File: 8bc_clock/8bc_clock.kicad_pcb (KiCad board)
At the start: 2 copper layers, 61 x 63.5 mm, 27 parts, among them J1 Conn_01x05_Pin, SW1 SW_SPDT, SW2 SW_DIP_x01, U1 ICM7555xP, U2 ICM7555xP, U3 ICM7555xP, U4 74LS04, U5 74LS08, U6 74LS32

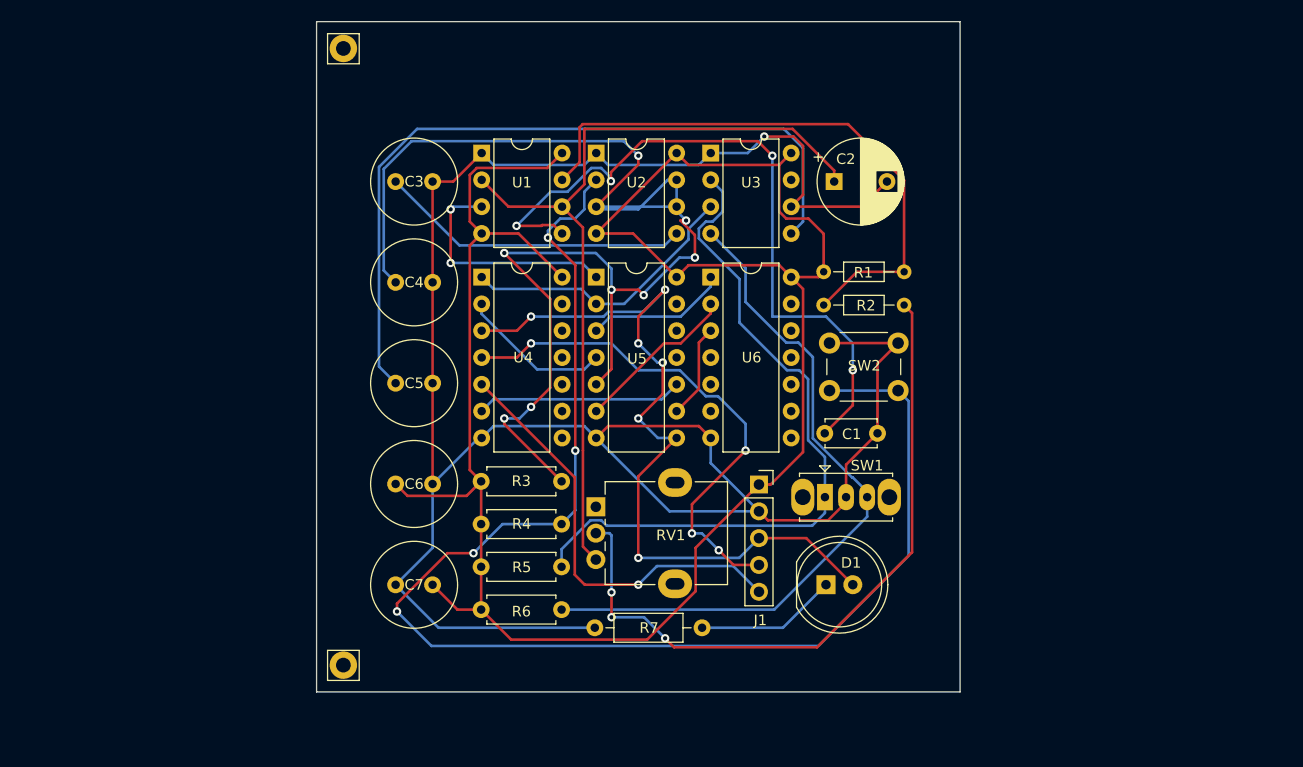
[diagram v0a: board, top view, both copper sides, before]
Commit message: fixed clock circuit error
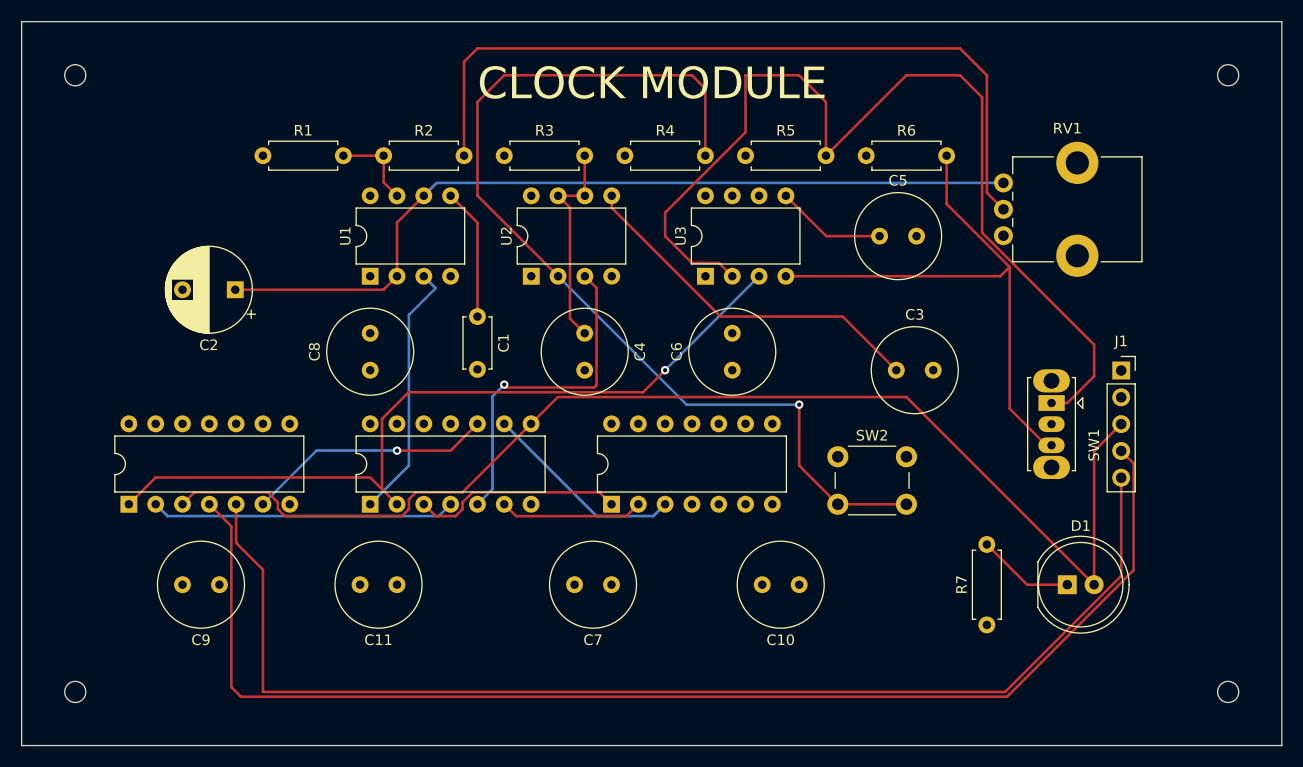
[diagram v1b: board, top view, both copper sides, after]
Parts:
- removed the REF** at (106.7, 53.3)
- removed the REF*** at (106.7, 111.8)
- added C10: 100n, Capacitor_THT:C_Radial_D8.0mm_H7.0mm_P3.50mm, F.Cu at (149.9, 104.1)
- added C11: 100n, Capacitor_THT:C_Radial_D8.0mm_H7.0mm_P3.50mm, F.Cu at (111.8, 104.1)
- added C8: 100n, Capacitor_THT:C_Radial_D8.0mm_H7.0mm_P3.50mm, F.Cu at (109.2, 83.8)
- added C9: 100n, Capacitor_THT:C_Radial_D8.0mm_H7.0mm_P3.50mm, F.Cu at (94.9, 104.1)
- added REF**: MountingHole_2mm, MountingHole:MountingHole_2mm, F.Cu at (81.3, 114.3)
- added REF**: MountingHole_2mm, MountingHole:MountingHole_2mm, F.Cu at (190.5, 55.9)
- added REF**: MountingHole_2mm, MountingHole:MountingHole_2mm, F.Cu at (190.5, 114.3)
- added REF***: MountingHole_2mm, MountingHole:MountingHole_2mm, F.Cu at (81.3, 55.9)
- C1, C3: value 0.01uF -> 10n
- C2: value 1uF -> 1u
- C4, C5, C6, C7: value 0.1uF -> 100n
- R1, R2: footprint Resistor_THT:R_Axial_DIN0204_L3.6mm_D1.6mm_P7.62mm_Horizontal -> Resistor_THT:R_Axial_DIN0207_L6.3mm_D2.5mm_P7.62mm_Horizontal
- R7: value 200 -> 220; footprint Resistor_THT:R_Axial_DIN0207_L6.3mm_D2.5mm_P10.16mm_Horizontal -> Resistor_THT:R_Axial_DIN0207_L6.3mm_D2.5mm_P7.62mm_Horizontal
- RV1: footprint Potentiometer_THT:Potentiometer_Alpha_RD901F-40-00D_Single_Vertical -> Potentiometer_THT:Potentiometer_Bourns_PTV09A-1_Single_Vertical
- moved C2 57.7 mm to (96.4, 76.2), turned to 180 degrees
- moved R6 56.4 mm to (156.2, 63.5)
- moved R1 54.2 mm to (99.1, 63.5)
- moved C3 50.7 mm to (159.1, 83.8)
- moved C5 47.9 mm to (157.5, 71.1)
- moved RV1 46.4 mm to (169.2, 71.1)
- moved R5 46.3 mm to (144.8, 63.5)
- moved R2 44.0 mm to (110.5, 63.5)
- moved U4 39.7 mm to (86.4, 96.5), turned to 90 degrees
- moved R4 37.5 mm to (133.3, 63.5)
- moved R7 37.1 mm to (167.6, 108.0), turned to 90 degrees
- moved J1 36.0 mm to (180.4, 83.8)
- moved C1 34.7 mm to (119.4, 78.7), turned to -90 degrees
- moved C6 33.7 mm to (143.5, 83.8), turned to 90 degrees
- moved R3 30.9 mm to (121.9, 63.5)
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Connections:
- C7 pad 1: GND -> +5V
- C7 pad 2: +5V -> GND
- U2 pad 3: Net-(U2-DIS) -> Net-(U2-Q)
- U5 pad 5: Net-(U2-DIS) -> Net-(U2-Q)
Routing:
- net GND: track 205.7 -> 0.00 mm, vias 1 -> 0
- net +5V: track 194.7 -> 0.00 mm
- net Net-(U2-DIS): track 128.9 -> 20.4 mm, vias 8 -> 0
- net HLT: track 41.3 -> 114.0 mm, vias 1 -> 0
- net !CLK: track 48.8 -> 120.8 mm, vias 4 -> 0
- net Net-(U3-CV): track 72.1 -> 10.5 mm
- net Net-(U1-CV): track 68.1 -> 12.5 mm, vias 4 -> 0
- net Net-(U3-Q): track 27.2 -> 75.5 mm, vias 0 -> 1
- net Net-(U1-DIS): track 56.3 -> 8.14 mm
- net CLK: track 74.6 -> 117.0 mm, vias 6 -> 0
- net Net-(U2-TR): track 132.3 -> 94.5 mm, vias 4 -> 1
- net Net-(U2-Q): track 0.00 -> 32.1 mm, vias 0 -> 1
- net Net-(SW1-A): track 67.4 -> 94.8 mm
- net Net-(U4-Pad2): track 14.4 -> 28.9 mm
- net Net-(SW1-C): track 66.3 -> 53.4 mm
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- added copper zone on In2.Cu, net +5V
- added copper zone on In1.Cu, net GND
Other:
- board size 61 x 63.5 mm -> 119.4 x 68.6 mm
- copper layers 2 -> 4
